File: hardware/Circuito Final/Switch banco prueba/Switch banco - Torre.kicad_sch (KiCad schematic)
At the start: 6 parts, among them J1 Conn_01x04_Socket, Q1_1 MMBT2222A

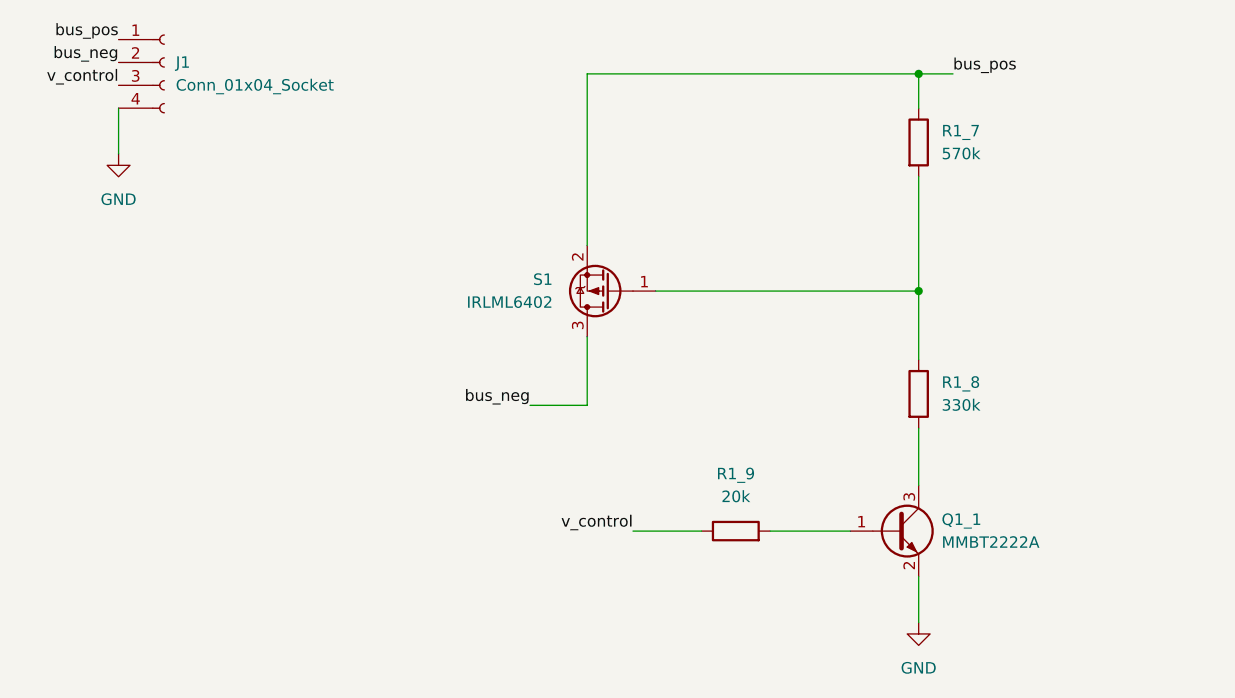
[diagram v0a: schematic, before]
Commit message: update menor del pcb de las celdas
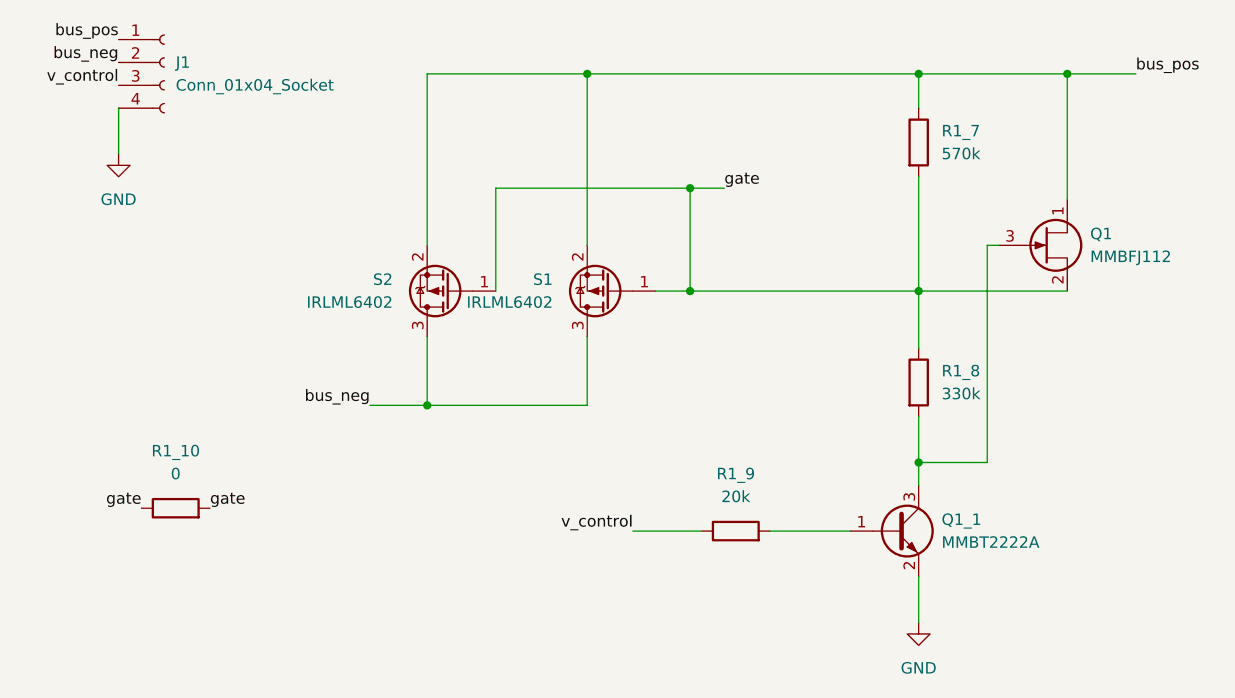
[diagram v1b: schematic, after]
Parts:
- added Q1: MMBFJ112, Package_TO_SOT_SMD:SOT-23, symbol Transistor_FET:MMBFJ112
- added R1_10: 0, Resistor_SMD:R_1206_3216Metric_Pad1.30x1.75mm_HandSolder, symbol Device:R
- added S2: IRLML6402, Package_TO_SOT_SMD:SOT-23, symbol Transistor_FET:IRLML6402
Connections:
- net bus_neg: now also S2.3 (D)
- net bus_pos: now also Q1.1 (D), S2.2 (S)
- net gate: now reaches R1_7.2, R1_8.1, S1.1 (G)
- net gate: now also Q1.2 (S), R1_10.1, R1_10.2, S2.1 (G)
- net at Q1_1.3 (C), R1_8.2: now also Q1.3 (G)
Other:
- moved on the sheet: R1_8

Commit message: update pcb celda y prueba del banco
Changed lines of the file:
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@@
 	)
 	(label "gate"
-		(at 99.06 88.9 0)
+		(at 120.65 90.17 0)
 		(effects
 			(font
@@
 			)
 			(justify left bottom)
+		)
+	)
+	(label "gate"
+		(at 113.03 90.17 180)
+		(effects
+			(font
+				(size 1.27 1.27)
+			)
+			(justify right bottom)
 		)
 	)
@@
 		)
 	)
-	(label "gate"
-		(at 91.44 88.9 180)
-		(effects
-			(font
-				(size 1.27 1.27)
-			)
-			(justify right bottom)
-		)
-	)
 	(label "bus_neg"
 		(at 116.84 77.47 180)
@@
 	)
 	(symbol
+		(lib_id "Device:R")
+		(at 116.84 90.17 90)
+		(unit 1)
+		(body_style 1)
+		(exclude_from_sim no)
+		(in_bom yes)
+		(on_board yes)
+		(in_pos_files yes)
+		(dnp no)
+		(fields_autoplaced yes)
+		(property "Reference" "R1_10"
+			(at 116.84 83.82 90)
+			(show_name no)
+			(do_not_autoplace no)
+			(effects
+				(font
+					(size 1.27 1.27)
+				)
+			)
+		)
+		(property "Value" "0"
+			(at 116.84 86.36 90)
+			(show_name no)
+			(do_not_autoplace no)
+			(effects
+				(font
+					(size 1.27 1.27)
+				)
+			)
+		)
+		(property "Footprint" "Resistor_SMD:R_1206_3216Metric_Pad1.30x1.75mm_HandSolder"
+			(at 116.84 91.948 90)
+			(hide yes)
+			(show_name no)
+			(do_not_autoplace no)
+			(effects
+				(font
+					(size 1.27 1.27)
+				)
+			)
+		)
+		(property "Datasheet" ""
+			(at 116.84 90.17 0)
+			(hide yes)
+			(show_name no)
+			(do_not_autoplace no)
+			(effects
+				(font
+					(size 1.27 1.27)
+				)
+			)
+		)
+		(property "Description" "Resistor"
+			(at 116.84 90.17 0)
+			(hide yes)
+			(show_name no)
+			(do_not_autoplace no)
+			(effects
+				(font
+					(size 1.27 1.27)
+				)
+			)
+		)
+		(pin "1"
+		)
+		(pin "2"
+		)
+		(instances
+			(project "Switch banco - Torre"
+				(path "/0f6cbaa3-1a93-4070-b53f-b642439dda2a"
+					(reference "R1_10")
+					(unit 1)
+				)
+			)
+		)
+	)
+	(symbol
 		(lib_id "power:GND")
 		(at 88.9 49.53 0)
@@
 					(unit 1)
 				)
-			)
-		)
-	)
-	(symbol
-		(lib_id "Device:R")
-		(at 95.25 88.9 90)
-		(unit 1)
-		(body_style 1)
-		(exclude_from_sim no)
-		(in_bom yes)
-		(on_board yes)
-		(in_pos_files yes)
-		(dnp no)
-		(fields_autoplaced yes)
-		(property "Reference" "R1_10"
-			(at 95.25 82.55 90)
-			(show_name no)
-			(do_not_autoplace no)
-			(effects
-				(font
-					(size 1.27 1.27)
-				)
-			)
-		)
-		(property "Value" "0"
-			(at 95.25 85.09 90)
-			(show_name no)
-			(do_not_autoplace no)
-			(effects
-				(font
-					(size 1.27 1.27)
-				)
-			)
-		)
-		(property "Footprint" "Resistor_SMD:R_1206_3216Metric_Pad1.30x1.75mm_HandSolder"
-			(at 95.25 90.678 90)
-			(hide yes)
-			(show_name no)
-			(do_not_autoplace no)
-			(effects
-				(font
-					(size 1.27 1.27)
-				)
-			)
-		)
-		(property "Datasheet" ""
-			(at 95.25 88.9 0)
-			(hide yes)
-			(show_name no)
-			(do_not_autoplace no)
-			(effects
-				(font
-					(size 1.27 1.27)
-				)
-			)
-		)
-		(property "Description" "Resistor"
-			(at 95.25 88.9 0)
-			(hide yes)
-			(show_name no)
-			(do_not_autoplace no)
-			(effects
-				(font
-					(size 1.27 1.27)
-				)
-			)
-		)
-		(pin "1"
-		)
-		(pin "2"
-		)
-		(instances
-			(project "Switch banco - Torre"
-				(path "/0f6cbaa3-1a93-4070-b53f-b642439dda2a"
-					(reference "R1_10")
-					(unit 1)
-				)
